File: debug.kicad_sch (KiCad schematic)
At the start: 84 parts, among them J8 USB4105-GF-A, J9 0878311420, Q10 DTC014TEBTL, Q11 DTC014TEBTL, Q12 DTC014TEBTL, U37 WE-TVS-82400152, U39 93LC66BT-IMC, U40 FT4232HPQ, U41 TPD4E05U06QDQARQ1_PASS, U42 74AVC4T245RSVRG4, U43 74AVC4T245RSVRG4, U44 SN74AVC2T245RSWR, U45 SN74AVC2T245RSWR, U46 NC7WZ07P6X, Y7 ABM8G-12.000MHZ-18-D2Y-T

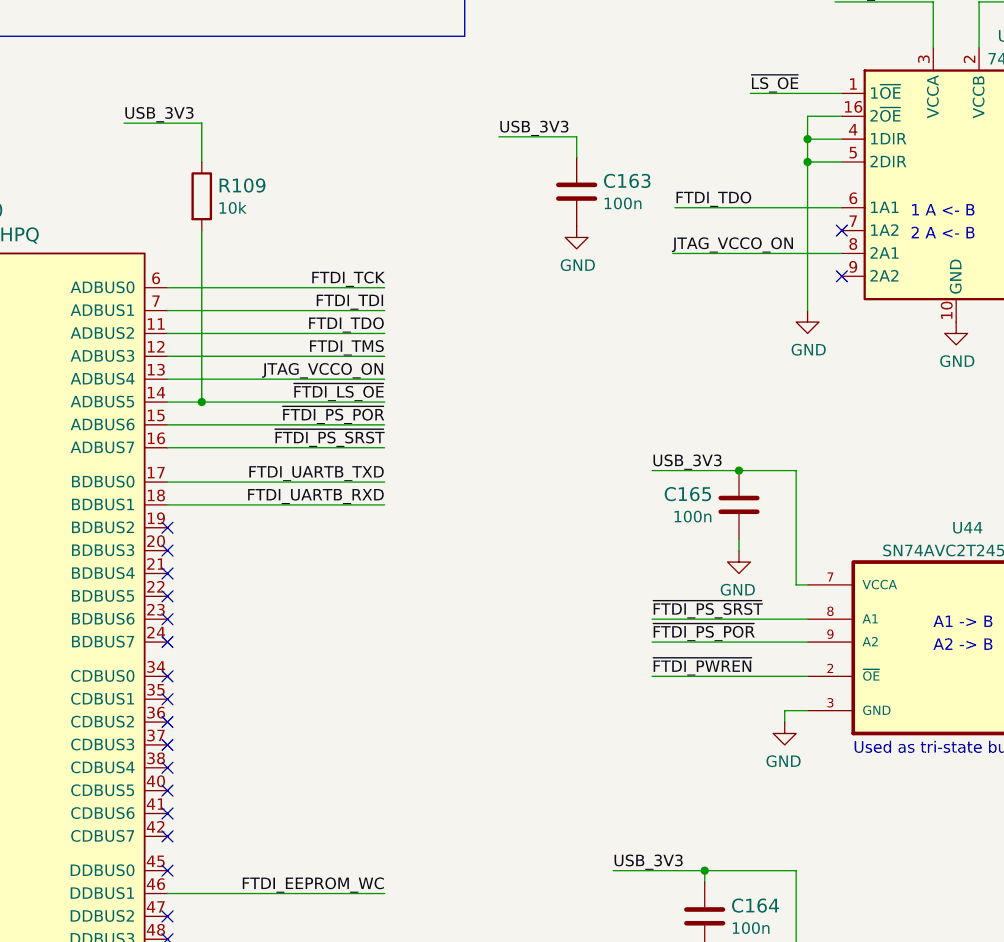
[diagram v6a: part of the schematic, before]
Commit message: Add test points on FTDI CDBUS
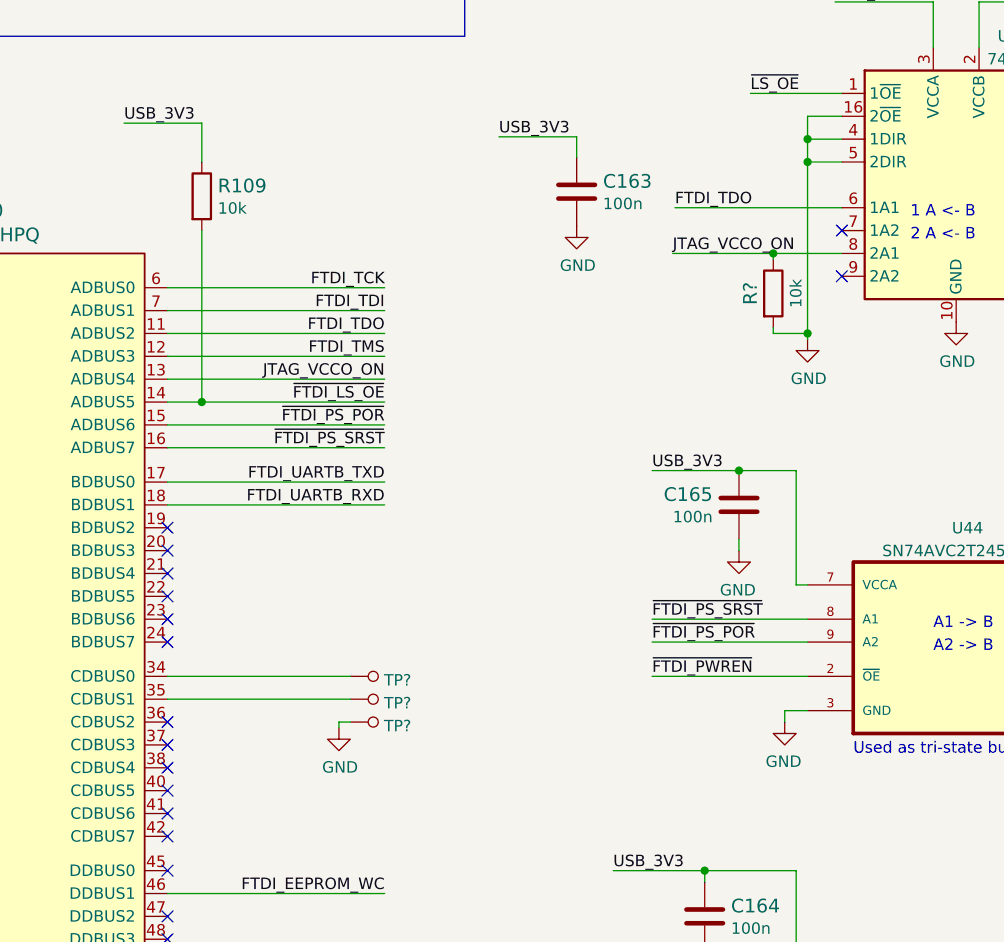
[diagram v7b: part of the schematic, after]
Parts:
- added R?: R_10k_0402, antmicro-footprints:0402-res, symbol antmicroResistors0402:R_10k_0402
- added TP? (x3): TP_SMD_0_75MM, antmicro-footprints:Testpoint_smd_0_75mm, symbol antmicroTestPoints:TP_SMD_0_75MM
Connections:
- net GND: now also R?.2, TP?.1
- net JTAG_VCCO_ON: now also R?.1
- net at U40.34 (CDBUS0): now also TP?.1
- net at U40.35 (CDBUS1): now also TP?.1
- no-connect marks 38 -> 36
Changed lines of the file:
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@@
   (junction (at 167.64 269.24) (diameter 0) (color 0 0 0 0)
   )
+  (junction (at 298.45 120.65) (diameter 0) (color 0 0 0 0)
+  )
   (junction (at 340.106 137.16) (diameter 0) (color 0 0 0 0)
   )
@@
   (junction (at 218.44 266.7) (diameter 0) (color 0 0 0 0)
   )
+  (junction (at 294.64 111.76) (diameter 0) (color 0 0 0 0)
+  )
   (junction (at 217.17 49.53) (diameter 0) (color 0 0 0 0)
   )
@@
   (no_connect (at 326.39 66.04))
   (no_connect (at 227.33 149.86))
-  (no_connect (at 227.33 158.75))
   (no_connect (at 227.33 163.83))
   (no_connect (at 118.11 60.96))
@@
   (no_connect (at 62.23 46.99))
   (no_connect (at 227.33 198.12))
-  (no_connect (at 227.33 161.29))
   (no_connect (at 227.33 185.42))
   (no_connect (at 227.33 176.53))
@@
     (stroke (width 0) (type default) (color 0 0 0 0))
   )
+  (wire (pts (xy 227.33 158.75) (xy 247.65 158.75))
+    (stroke (width 0) (type default) (color 0 0 0 0))
+  )
+  (wire (pts (xy 246.38 164.465) (xy 246.38 163.83))
+    (stroke (width 0) (type default) (color 0 0 0 0))
+  )
   (wire (pts (xy 322.834 36.322) (xy 316.23 36.322))
     (stroke (width 0) (type default) (color 0 0 0 0))
@@
     (stroke (width 0) (type default) (color 0 0 0 0))
   )
-  (wire (pts (xy 283.464 111.76) (xy 302.26 111.76))
+  (wire (pts (xy 283.464 111.76) (xy 294.64 111.76))
     (stroke (width 0) (type default) (color 0 0 0 0))
   )
@@
     (stroke (width 0) (type default) (color 0 0 0 0))
   )
+  (wire (pts (xy 246.38 163.83) (xy 247.65 163.83))
+    (stroke (width 0) (type default) (color 0 0 0 0))
+  )
   (wire (pts (xy 335.28 161.29) (xy 335.28 158.75))
     (stroke (width 0) (type default) (color 0 0 0 0))
@@
     (stroke (width 0) (type default) (color 0 0 0 0))
   )
+  (wire (pts (xy 298.45 120.65) (xy 298.45 121.285))
+    (stroke (width 0) (type default) (color 0 0 0 0))
+  )
   (wire (pts (xy 227.33 123.19) (xy 251.46 123.19))
     (stroke (width 0) (type default) (color 0 0 0 0))
@@
     (stroke (width 0) (type default) (color 0 0 0 0))
   )
+  (wire (pts (xy 294.64 120.65) (xy 298.45 120.65))
+    (stroke (width 0) (type default) (color 0 0 0 0))
+  )
   (wire (pts (xy 26.416 147.32) (xy 36.83 147.32))
     (stroke (width 0) (type default) (color 0 0 0 0))
   )
+  (wire (pts (xy 294.64 120.015) (xy 294.64 120.65))
+    (stroke (width 0) (type default) (color 0 0 0 0))
+  )
   (wire (pts (xy 185.42 147.32) (xy 186.69 147.32))
     (stroke (width 0) (type default) (color 0 0 0 0))
@@
     (stroke (width 0) (type default) (color 0 0 0 0))
   )
-  (wire (pts (xy 298.45 101.6) (xy 298.45 118.11))
+  (wire (pts (xy 298.45 101.6) (xy 298.45 120.65))
     (stroke (width 0) (type default) (color 0 0 0 0))
   )
@@
     (stroke (width 0) (type default) (color 0 0 0 0))
   )
+  (wire (pts (xy 294.64 111.76) (xy 302.26 111.76))
+    (stroke (width 0) (type default) (color 0 0 0 0))
+  )
   (wire (pts (xy 334.01 158.75) (xy 335.28 158.75))
     (stroke (width 0) (type default) (color 0 0 0 0))
@@
     (stroke (width 0) (type default) (color 0 0 0 0))
   )
+  (wire (pts (xy 294.64 111.76) (xy 294.64 112.395))
+    (stroke (width 0) (type default) (color 0 0 0 0))
+  )
   (wire (pts (xy 54.61 224.536) (xy 67.564 224.536))
     (stroke (width 0) (type default) (color 0 0 0 0))
@@
     (stroke (width 0) (type default) (color 0 0 0 0))
   )
+  (wire (pts (xy 227.33 161.29) (xy 247.65 161.29))
+    (stroke (width 0) (type default) (color 0 0 0 0))
+  )
   (wire (pts (xy 298.45 96.52) (xy 302.26 96.52))
     (stroke (width 0) (type default) (color 0 0 0 0))
@@
     (pin "1")
   )
-  (symbol (lib_id "kria-k26-devboard:GND") (at 298.45 118.11 0) (unit 1)
+  (symbol (lib_id "kria-k26-devboard:GND") (at 298.45 121.285 0) (unit 1)
     (in_bom yes) (on_board yes)
-    (property "Reference" "#PWR0351" (id 0) (at 298.45 124.46 0)
+    (property "Reference" "#PWR0351" (id 0) (at 298.45 127.635 0)
       (effects (font (size 1.27 1.27)) hide)
     )
-    (property "Value" "GND" (id 1) (at 298.577 122.5042 0))
-    (property "Footprint" "" (id 2) (at 298.45 118.11 0)
+    (property "Value" "GND" (id 1) (at 298.577 125.6792 0))
+    (property "Footprint" "" (id 2) (at 298.45 121.285 0)
       (effects (font (size 1.27 1.27)) hide)
     )
-    (property "Datasheet" "" (id 3) (at 298.45 118.11 0)
+    (property "Datasheet" "" (id 3) (at 298.45 121.285 0)
       (effects (font (size 1.27 1.27)) hide)
     )
@@
     (pin "9")
   )
+  (symbol (lib_id "antmicroTestPoints:TP_SMD_0_75MM") (at 250.19 158.75 90) (unit 1)
+    (in_bom yes) (on_board yes) (fields_autoplaced)
+    (property "Reference" "TP?" (id 0) (at 251.3838 159.1838 90)
+      (effects (font (size 1.27 1.27)) (justify right))
+    )
+    (property "Value" "TP_SMD_0_75MM" (id 1) (at 252.73 158.75 0)
+      (effects (font (size 1.27 1.27)) hide)
+    )
+    (property "Footprint" "antmicro-footprints:Testpoint_smd_0_75mm" (id 2) (at 245.11 153.67 0)
+      (effects (font (size 1.524 1.524)) (justify left) hide)
+    )
+    (property "Datasheet" "" (id 3) (at 242.57 153.67 0)
+      (effects (font (size 1.524 1.524)) (justify left) hide)
+    )
+    (pin "1")
+  )
   (symbol (lib_id "antmicroCapacitors0603:C_1u_0603_25V") (at 93.345 64.135 0) (unit 1)
     (in_bom yes) (on_board yes) (fields_autoplaced)
@@
     (pin "2")
   )
+  (symbol (lib_id "antmicroResistors0402:R_10k_0402") (at 294.64 116.205 270) (unit 1)
+    (in_bom yes) (on_board yes)
+    (property "Reference" "R?" (id 0) (at 292.1 116.205 0)
+      (effects (font (size 1.524 1.524)))
+    )
+    (property "Value" "R_10k_0402" (id 1) (at 290.83 116.205 0)
+      (effects (font (size 1.524 1.524)) hide)
+    )
+    (property "Footprint" "antmicro-footprints:0402-res" (id 2) (at 299.72 121.285 0)
+      (effects (font (size 1.524 1.524)) (justify left) hide)
+    )
+    (property "Datasheet" "" (id 3) (at 294.64 116.205 0)
+      (effects (font (size 1.27 1.27)) hide)
+    )
+    (property "Manufacturer" "VISHAY" (id 4) (at 304.8 121.285 0)
+      (effects (font (size 1.524 1.524)) (justify left) hide)
+    )
+    (property "MPN" "CRCW040210K0FKEDHP" (id 5) (at 302.26 121.285 0)
+      (effects (font (size 1.524 1.524)) (justify left) hide)
+    )
+    (property "Val" "10k" (id 6) (at 297.18 116.205 0))
+    (pin "1")
+    (pin "2")
+  )
+  (symbol (lib_id "kria-k26-devboard:GND") (at 246.38 164.465 0) (unit 1)
+    (in_bom yes) (on_board yes)
+    (property "Reference" "#PWR?" (id 0) (at 246.38 170.815 0)
+      (effects (font (size 1.27 1.27)) hide)
+    )
+    (property "Value" "GND" (id 1) (at 246.507 168.8592 0))
+    (property "Footprint" "" (id 2) (at 246.38 164.465 0)
+      (effects (font (size 1.27 1.27)) hide)
+    )
+    (property "Datasheet" "" (id 3) (at 246.38 164.465 0)
+      (effects (font (size 1.27 1.27)) hide)
+    )
+    (pin "1")
+  )
   (symbol (lib_id "kria-k26-devboard:GND") (at 122.555 68.58 0) (unit 1)
     (in_bom yes) (on_board yes)
@@
     (pin "1")
   )
+  (symbol (lib_id "antmicroTestPoints:TP_SMD_0_75MM") (at 250.19 161.29 90) (unit 1)
+    (in_bom yes) (on_board yes) (fields_autoplaced)
+    (property "Reference" "TP?" (id 0) (at 251.3838 161.7238 90)
+      (effects (font (size 1.27 1.27)) (justify right))
+    )
+    (property "Value" "TP_SMD_0_75MM" (id 1) (at 252.73 161.29 0)
+      (effects (font (size 1.27 1.27)) hide)
+    )
+    (property "Footprint" "antmicro-footprints:Testpoint_smd_0_75mm" (id 2) (at 245.11 156.21 0)
+      (effects (font (size 1.524 1.524)) (justify left) hide)
+    )
+    (property "Datasheet" "" (id 3) (at 242.57 156.21 0)
+      (effects (font (size 1.524 1.524)) (justify left) hide)
+    )
+    (pin "1")
+  )
   (symbol (lib_id "antmicroCapacitors0603:C_1u_0603_25V") (at 94.615 36.195 0) (unit 1)
     (in_bom yes) (on_board yes) (fields_autoplaced)
@@
     (pin "2")
   )
+  (symbol (lib_id "antmicroTestPoints:TP_SMD_0_75MM") (at 250.19 163.83 90) (unit 1)
+    (in_bom yes) (on_board yes) (fields_autoplaced)
+    (property "Reference" "TP?" (id 0) (at 251.3838 164.2638 90)
+      (effects (font (size 1.27 1.27)) (justify right))
+    )
+    (property "Value" "TP_SMD_0_75MM" (id 1) (at 252.73 163.83 0)
+      (effects (font (size 1.27 1.27)) hide)
+    )
+    (property "Footprint" "antmicro-footprints:Testpoint_smd_0_75mm" (id 2) (at 245.11 158.75 0)
+      (effects (font (size 1.524 1.524)) (justify left) hide)
+    )
+    (property "Datasheet" "" (id 3) (at 242.57 158.75 0)
+      (effects (font (size 1.524 1.524)) (justify left) hide)
+    )
+    (pin "1")
+  )
 )

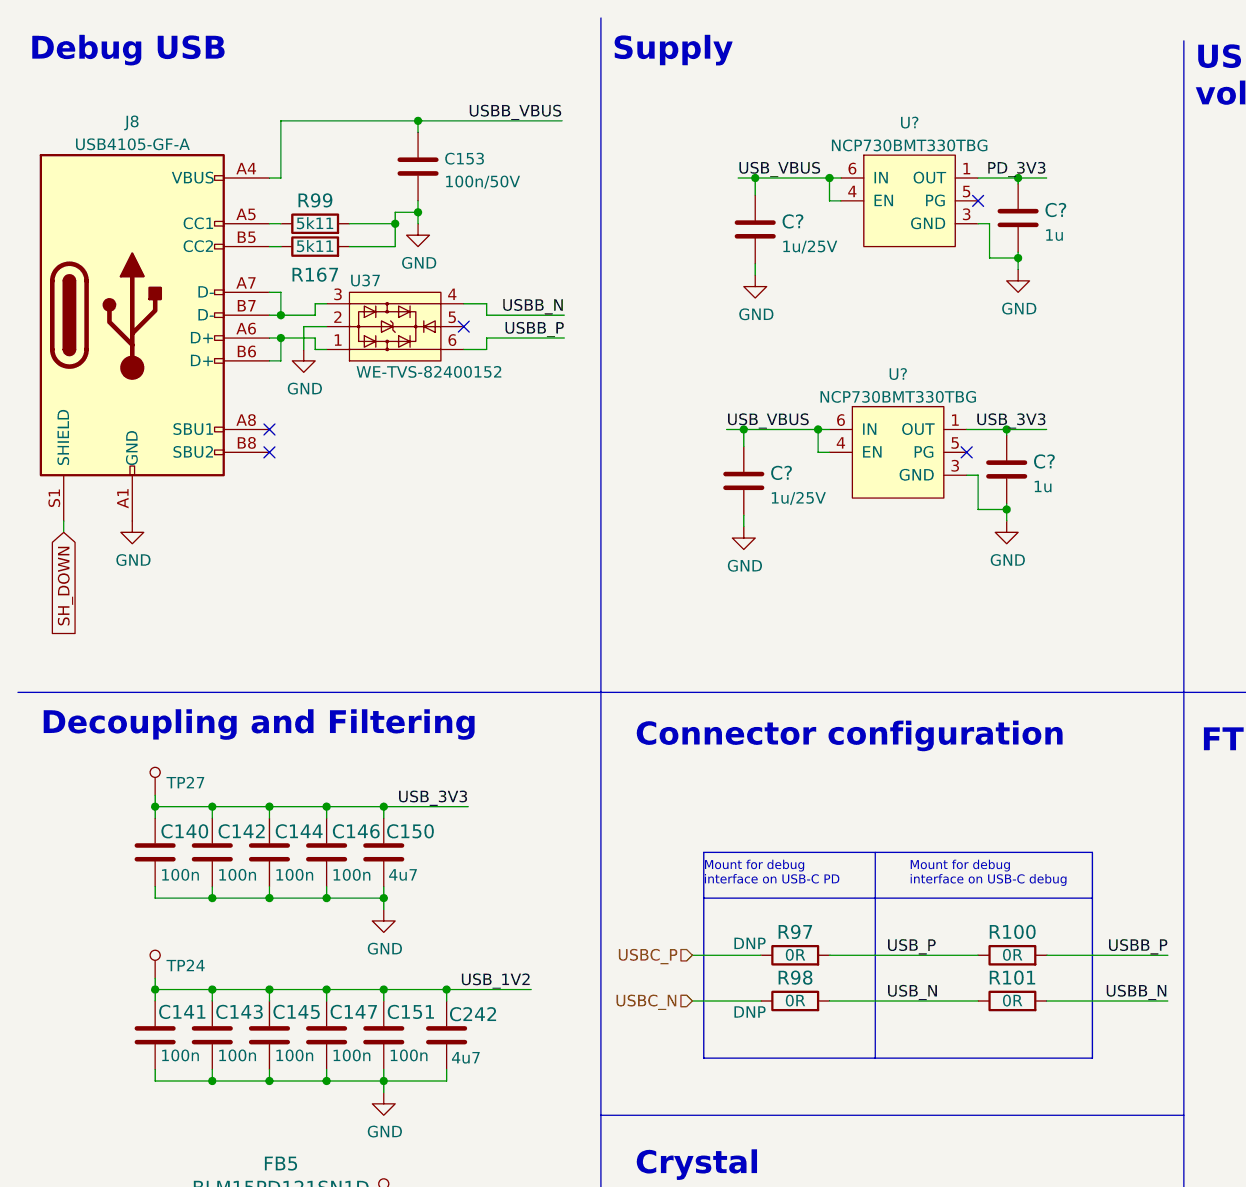
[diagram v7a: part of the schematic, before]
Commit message: Change USB debug connector to DNP by default
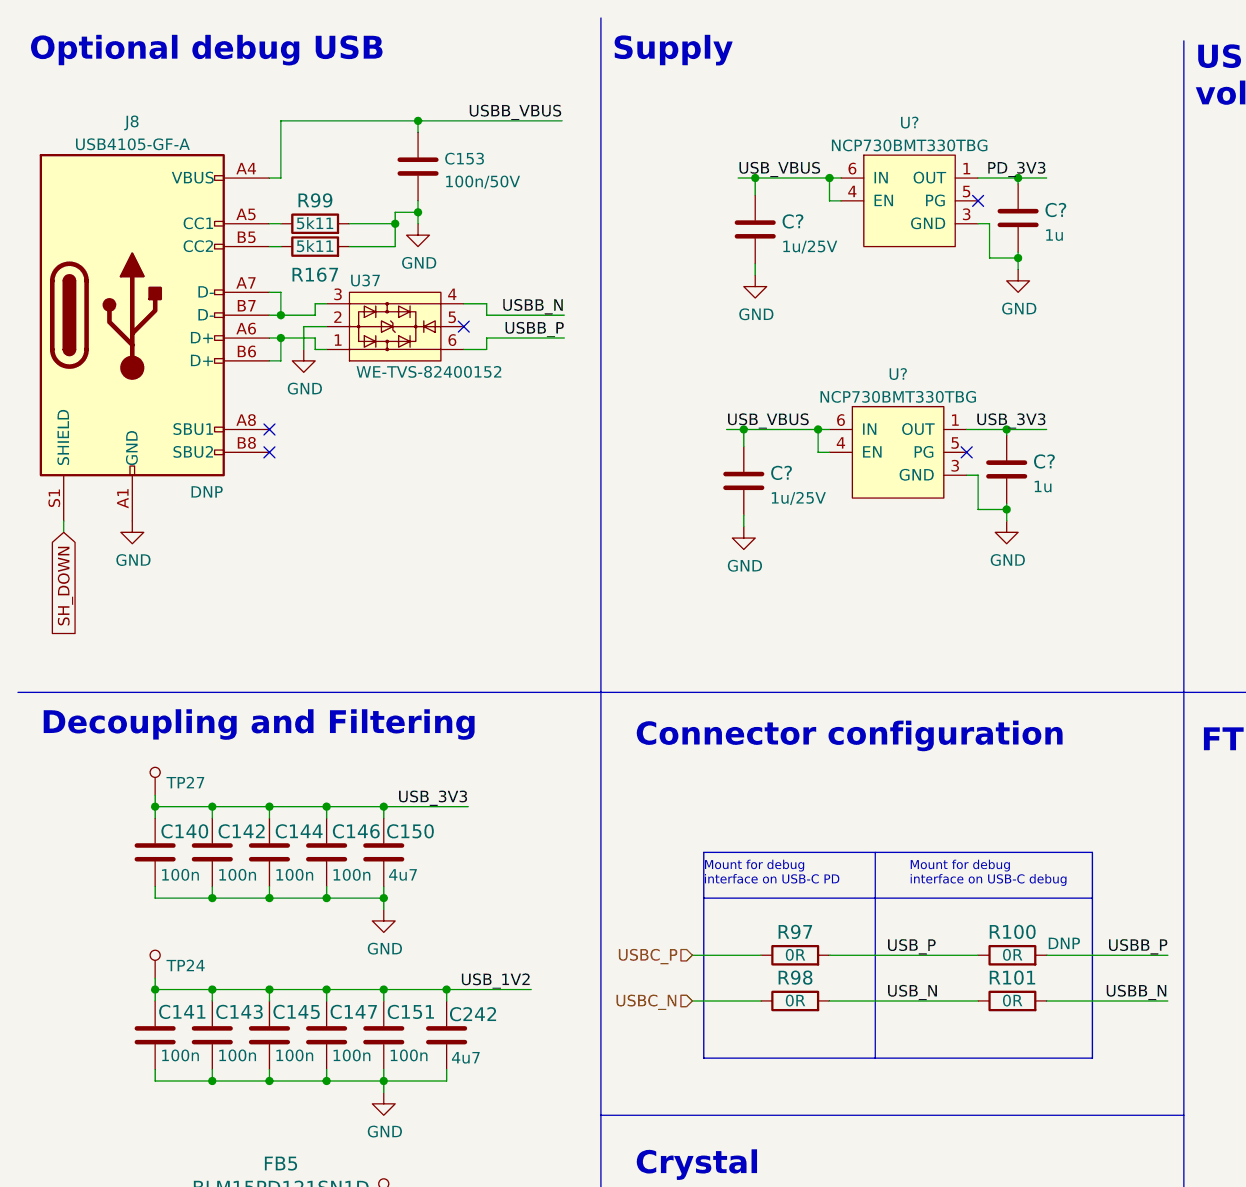
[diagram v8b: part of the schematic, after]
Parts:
- J8, R100: DNP (none) -> DNP
- R97, R98: DNP DNP -> (none)
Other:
- note added: "Optional debug USB"
- note removed: "Debug USB"
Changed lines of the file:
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@@
     (effects (font (size 2.54 2.54) (thickness 0.508) bold) (justify left bottom))
   )
-  (text "Debug USB" (at 13.97 17.78 0)
+  (text "Optional debug USB" (at 13.97 17.78 0)
     (effects (font (size 2.54 2.54) (thickness 0.508) bold) (justify left bottom))
   )
@@
   )
   (symbol (lib_id "kria-k26-devboard:USB4105-GF-A") (at 25.4 45.72 0) (unit 1)
-    (in_bom yes) (on_board yes) (fields_autoplaced)
+    (in_bom yes) (on_board yes)
     (property "Reference" "J8" (id 0) (at 25.4 24.2402 0))
     (property "Value" "USB4105-GF-A" (id 1) (at 25.4 26.7771 0))
@@
       (effects (font (size 1.27 1.27)) hide)
     )
+    (property "DNP" "DNP" (id 6) (at 33.655 65.405 0))
     (pin "A1")
     (pin "A12")
@@
     )
     (property "Val" "0R" (id 6) (at 99.06 116.84 0))
-    (property "DNP" "DNP" (id 7) (at 93.98 115.57 0))
     (pin "1")
     (pin "2")
@@
     )
     (property "Val" "0R" (id 6) (at 123.19 116.84 0))
+    (property "DNP" "DNP" (id 7) (at 128.905 115.57 0))
     (pin "1")
     (pin "2")
@@
     )
     (property "Val" "0R" (id 6) (at 99.06 121.92 0))
-    (property "DNP" "DNP" (id 7) (at 93.98 123.19 0))
-    (pin "1")
-    (pin "2")
+    (pin "1")
+    (pin "2")
